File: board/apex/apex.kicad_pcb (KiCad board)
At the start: 4 copper layers, 65.4 x 30.5 mm, 14 parts, among them J1 USB4125-GF-A_REVA2, U1 AP7363-33D-13

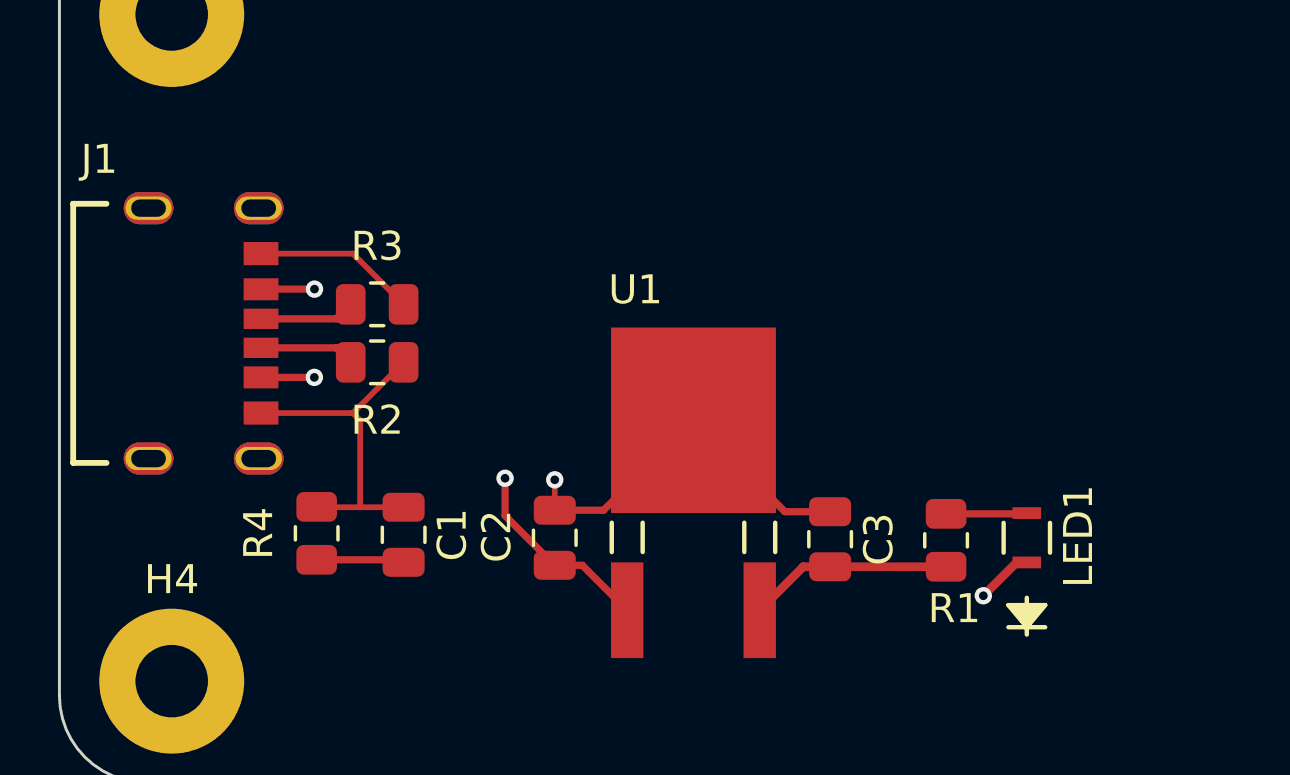
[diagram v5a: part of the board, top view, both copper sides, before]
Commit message: expanded LED pads
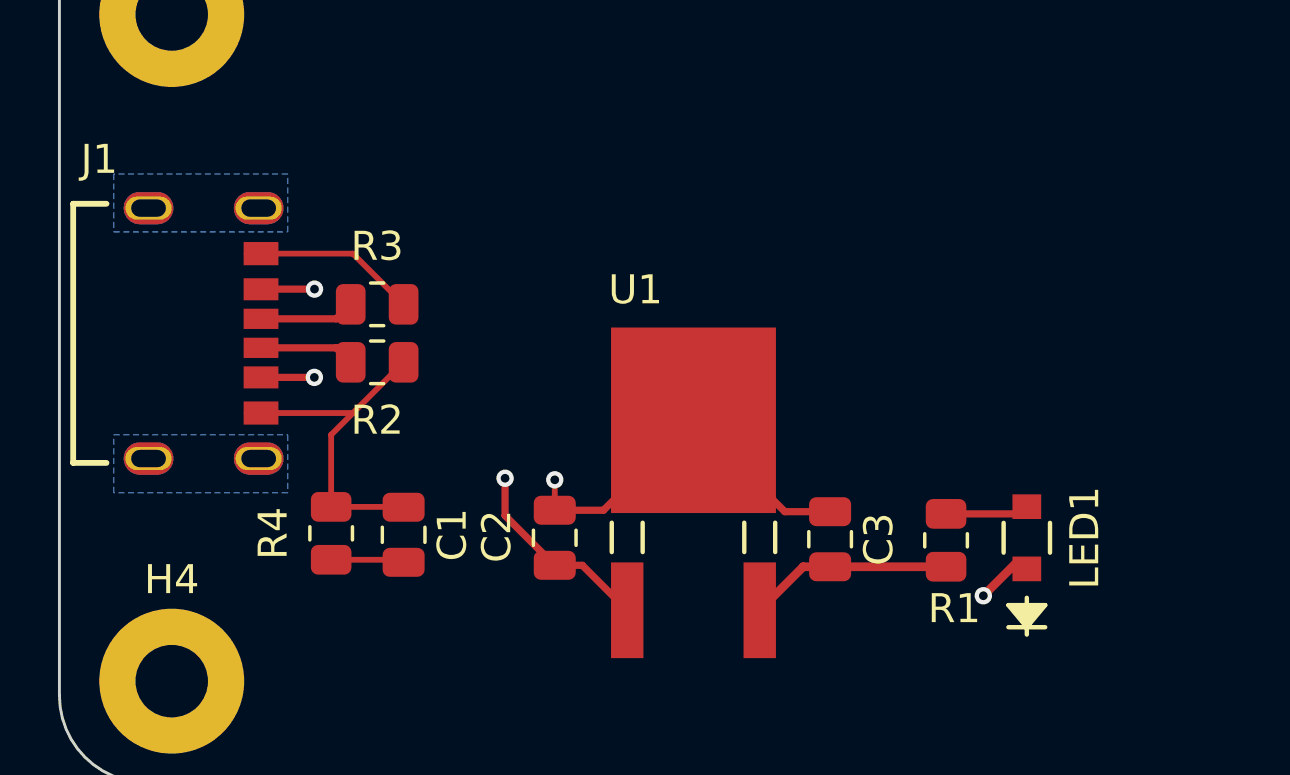
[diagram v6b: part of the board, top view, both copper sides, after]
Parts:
- moved R4 0.50 mm to (26.0, 52.9)
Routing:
- net GNDPWR: track 3.08 -> 2.58 mm
- added copper zone on In1.Cu, net GND
- added copper zone on B.Cu, net GNDPWR
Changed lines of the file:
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@@
 	(footprint "Resistor_SMD:R_0805_2012Metric"
 		(layer "F.Cu")
-		(at 25.5 52.9 -90)
+		(at 26 52.9 -90)
 		(descr "Resistor SMD 0805 (2012 Metric), square (rectangular) end terminal, IPC_7351 nominal, (Body size source: IPC-SM-782 page 72, https://www.pcb-3d.com/wordpress/wp-content/uploads/ipc-sm-782a_amendment_1_and_2.pdf), generated with kicad-footprint-generator")
 		(tags "resistor")
@@
 		(tags "150080BS75000 ")
 		(property "Reference" "LED1"
-			(at 0.0532 1.786 90)
+			(at 0 2 90)
 			(unlocked yes)
 			(layer "F.SilkS")
@@
 		)
 		(property "Value" "150080BS75000"
-			(at 0 0 90)
+			(at 0 -2 90)
 			(unlocked yes)
 			(layer "F.Fab")
@@
 		)
 		(fp_line
-			(start 1.3081 -0.9271)
-			(end 1.3081 -0.7493)
-			(stroke
-				(width 0.1524)
-				(type solid)
-			)
-			(layer "F.CrtYd")
-		)
-		(fp_line
-			(start -1.3081 -0.9271)
-			(end 1.3081 -0.9271)
-			(stroke
-				(width 0.1524)
-				(type solid)
-			)
-			(layer "F.CrtYd")
-		)
-		(fp_line
-			(start 1.3081 -0.7493)
-			(end 1.3081 -0.7493)
-			(stroke
-				(width 0.1524)
-				(type solid)
-			)
-			(layer "F.CrtYd")
-		)
-		(fp_line
-			(start 1.3081 -0.7493)
-			(end 1.3081 0.7493)
-			(stroke
-				(width 0.1524)
-				(type solid)
-			)
-			(layer "F.CrtYd")
-		)
-		(fp_line
-			(start -1.3081 -0.7493)
-			(end -1.3081 -0.9271)
-			(stroke
-				(width 0.1524)
-				(type solid)
-			)
-			(layer "F.CrtYd")
-		)
-		(fp_line
-			(start -1.3081 -0.7493)
-			(end -1.3081 -0.7493)
-			(stroke
-				(width 0.1524)
-				(type solid)
-			)
-			(layer "F.CrtYd")
-		)
-		(fp_line
-			(start 1.3081 0.7493)
-			(end 1.3081 0.7493)
+			(start -2 -0.9271)
+			(end 2 -0.9271)
 			(stroke
 				(width 0.1524)
@@
 		)
 		(fp_line
-			(start 1.3081 0.7493)
-			(end 1.3081 0.9271)
+			(start 2 -0.87465)
+			(end 2 0.87465)
 			(stroke
 				(width 0.1524)
@@
 		)
 		(fp_line
-			(start -1.3081 0.7493)
-			(end -1.3081 -0.7493)
+			(start -2 -0.7493)
+			(end -2 -0.9271)
 			(stroke
 				(width 0.1524)
@@
 		)
 		(fp_line
-			(start -1.3081 0.7493)
-			(end -1.3081 0.7493)
+			(start -2 0.7493)
+			(end -2 -0.7493)
 			(stroke
 				(width 0.1524)
@@
 		)
 		(fp_line
-			(start 1.3081 0.9271)
-			(end -1.3081 0.9271)
+			(start 2 0.9271)
+			(end -2 0.9271)
 			(stroke
 				(width 0.1524)
@@
 		)
 		(fp_line
-			(start -1.3081 0.9271)
-			(end -1.3081 0.7493)
+			(start -2 0.9271)
+			(end -2 0.7493)
 			(stroke
 				(width 0.1524)
@@
 		)
 		(fp_text user "${REFERENCE}"
-			(at 0 0 90)
+			(at 0 -4 90)
 			(unlocked yes)
 			(layer "F.Fab")
@@
 		)
 		(pad "1" smd rect
-			(at -0.8509 0 90)
-			(size 0.4064 0.9906)
+			(at -1.07385 0 90)
+			(size 0.8523 0.9906)
 			(layers "F.Cu" "F.Paste" "F.Mask")
 			(net 2 "GND")
@@
 		)
 		(pad "2" smd rect
-			(at 0.8509 0 90)
-			(size 0.4064 0.9906)
+			(at 1.07385 0 90)
+			(size 0.8523 0.9906)
 			(layers "F.Cu" "F.Paste" "F.Mask")
 			(net 7 "Net-(LED1-Pad2)")
@@
 	)
 	(segment
-		(start 27 49)
-		(end 26.75 48.75)
-		(width 0.2)
-		(layer "F.Cu")
-		(net 2)
-	)
-	(segment
-		(start 28.5 52)
-		(end 27 52)
+		(start 26 49.5)
+		(end 26 51.9875)
 		(width 0.2)
 		(layer "F.Cu")
@@
 	)
 	(segment
-		(start 27 52)
-		(end 27 49)
-		(width 0.2)
-		(layer "F.Cu")
-		(net 2)
-	)
-	(segment
-		(start 27 52)
-		(end 25.5125 52)
-		(width 0.2)
-		(layer "F.Cu")
-		(net 2)
-	)
-	(segment
 		(start 33.714 52.1032)
 		(end 33.714 51.0532)
@@
 	)
 	(segment
+		(start 26.75 48.75)
+		(end 26 49.5)
+		(width 0.2)
+		(layer "F.Cu")
+		(net 2)
+	)
+	(segment
 		(start 26.75 43.25)
 		(end 28.5 45)
@@
 		(net 2)
 	)
+	(segment
+		(start 28.4875 51.9875)
+		(end 28.5 52)
+		(width 0.2)
+		(layer "F.Cu")
+		(net 2)
+	)
+	(segment
+		(start 26 51.9875)
+		(end 28.4875 51.9875)
+		(width 0.2)
+		(layer "F.Cu")
+		(net 2)
+	)
 	(via blind
 		(at 33.714 51.0532)
@@
 	)
 	(segment
-		(start 25.5 53.8125)
-		(end 25.45488 53.8125)
-		(width 0.25)
+		(start 26 53.8125)
+		(end 28.4125 53.8125)
+		(width 0.2)
 		(layer "F.Cu")
 		(net 4)
@@
 	(segment
 		(start 25.5 53.8125)
-		(end 28.4125 53.8125)
+		(end 25.45488 53.8125)
 		(width 0.25)
 		(layer "F.Cu")
@@
 		(net 7)
 	)
+	(zone
+		(net 2)
+		(net_name "GND")
+		(layer "In1.Cu")
+		(hatch edge 0.5)
+		(connect_pads
+			(clearance 0.5)
+		)
+		(min_thickness 0.25)
+		(filled_areas_thickness no)
+		(fill yes
+			(thermal_gap 0.5)
+			(thermal_bridge_width 0.5)
+		)
+		(polygon
+			(pts
+				(xy 25 36) (xy 25 58) (xy 56 58.5) (xy 56 36)
+			)
+		)
+	)
+	(zone
+		(net 4)
+		(net_name "GNDPWR")
+		(layer "B.Cu")
+		(hatch edge 0.5)
+		(priority 2)
+		(connect_pads
+			(clearance 0.5)
+		)
+		(min_thickness 0.25)
+		(filled_areas_thickness no)
+		(fill yes
+			(thermal_gap 0.5)
+			(thermal_bridge_width 0.5)
+		)
+		(polygon
+			(pts
+				(xy 18.5 42.5) (xy 24.5 42.5) (xy 24.5 40.5) (xy 18.5 40.5)
+			)
+		)
+	)
+	(zone
+		(net 4)
+		(net_name "GNDPWR")
+		(layer "B.Cu")
+		(hatch edge 0.5)
+		(priority 1)
+		(connect_pads
+			(clearance 0.5)
+		)
+		(min_thickness 0.25)
+		(filled_areas_thickness no)
+		(fill yes
+			(thermal_gap 0.5)
+			(thermal_bridge_width 0.5)
+		)
+		(polygon
+			(pts
+				(xy 24.5 49.5) (xy 24.5 51.5) (xy 18.5 51.5) (xy 18.5 49.5)
+			)
+		)
+	)
 )

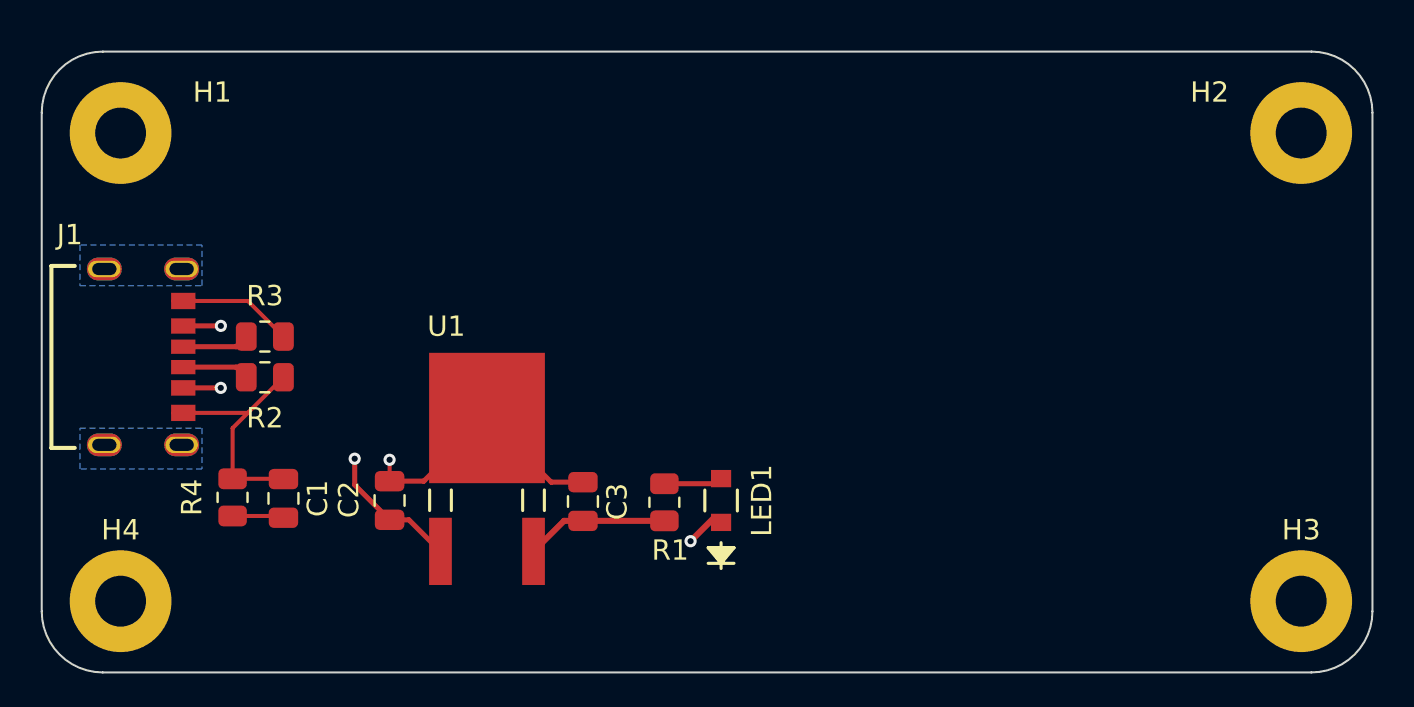
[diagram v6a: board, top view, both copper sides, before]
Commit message: added 3d models; added TVS diodes
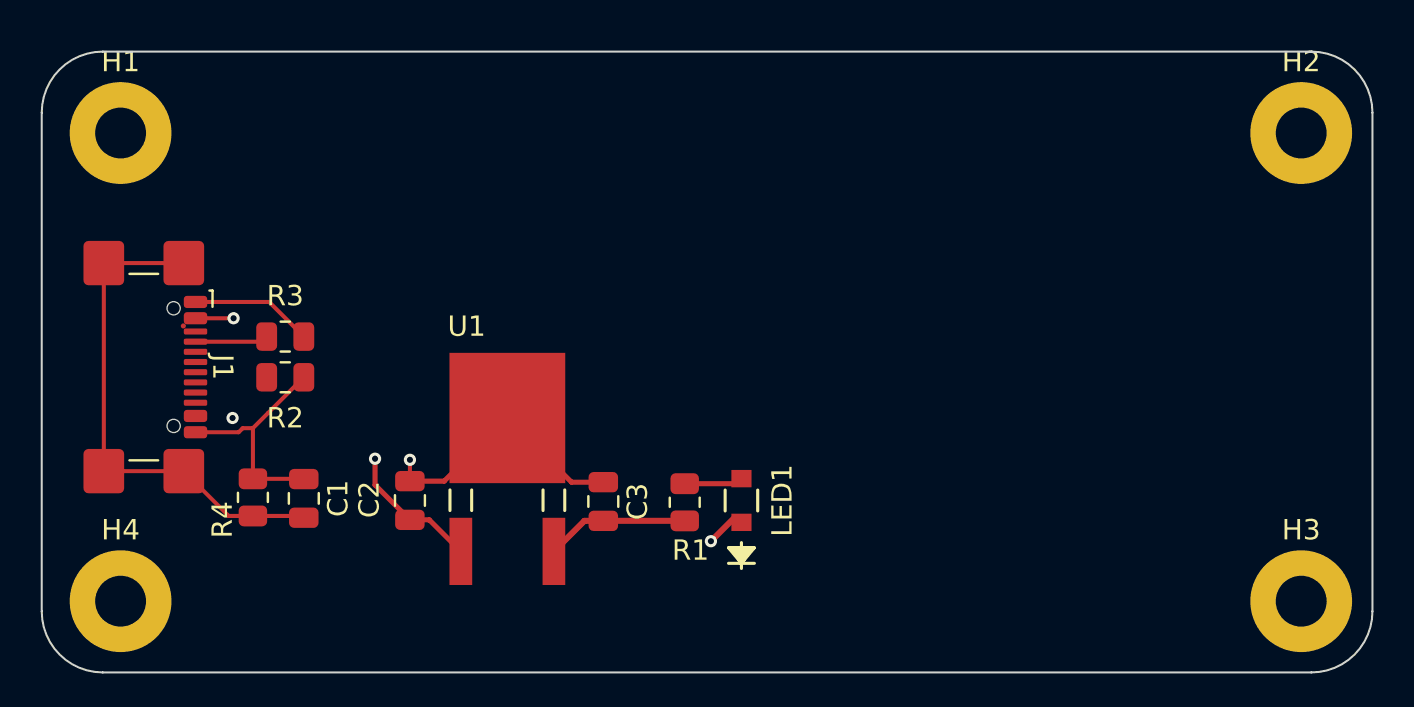
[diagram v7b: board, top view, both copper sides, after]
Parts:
- J1: value USB4125-GF-A_REVA2 -> USB_C_Receptacle_USB2.0_16P; footprint USB4125_GF_A:GCT_USB4125-GF-A_REVA2 -> Connector_USB:USB_C_Receptacle_GCT_USB4110
- moved C1 1.00 mm to (29.5, 53.0)
- moved C2 1.00 mm to (34.7, 53.1)
- moved C3 1.00 mm to (44.2, 53.1)
- moved LED1 1.00 mm to (51.0, 53.1)
- moved R1 1.00 mm to (48.2, 53.1)
- moved R2 1.00 mm to (28.6, 47.0)
- moved R3 1.00 mm to (28.6, 45.0)
- moved R4 1.00 mm to (27.0, 52.9)
- moved U1 1.00 mm to (39.5, 49.0)
- moved J1 0.50 mm to (20.5, 46.5)
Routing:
- net GNDPWR: track 2.58 -> 25.0 mm
- net Net-(J1-CC2): track 3.30 -> 0.00 mm
- net GND: track 49.9 -> 49.0 mm
- removed copper zone on In1.Cu, net GND
- removed copper zone on B.Cu, net GNDPWR
